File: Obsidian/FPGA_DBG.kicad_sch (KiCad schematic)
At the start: 24 parts, among them Q3 BSS138LT1G, SW1 SW_DIP_x01, U1 XC7A35T-CSG325, U27 W25Q128JVFIQ, U9 REF3012

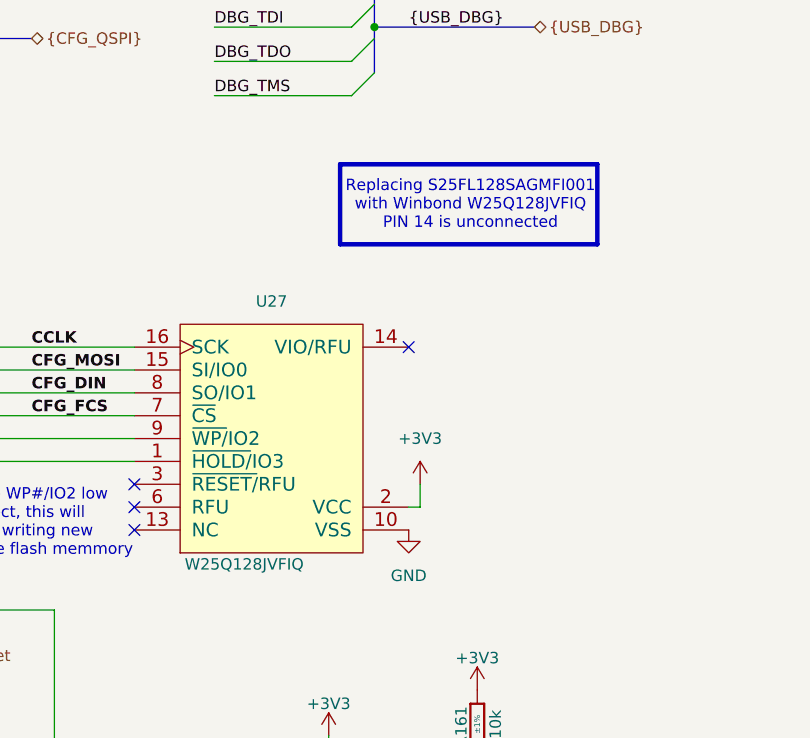
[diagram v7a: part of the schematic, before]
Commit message: Putting back S25FL128SAGMFI001 in FPGA_DBG sheet, see #17
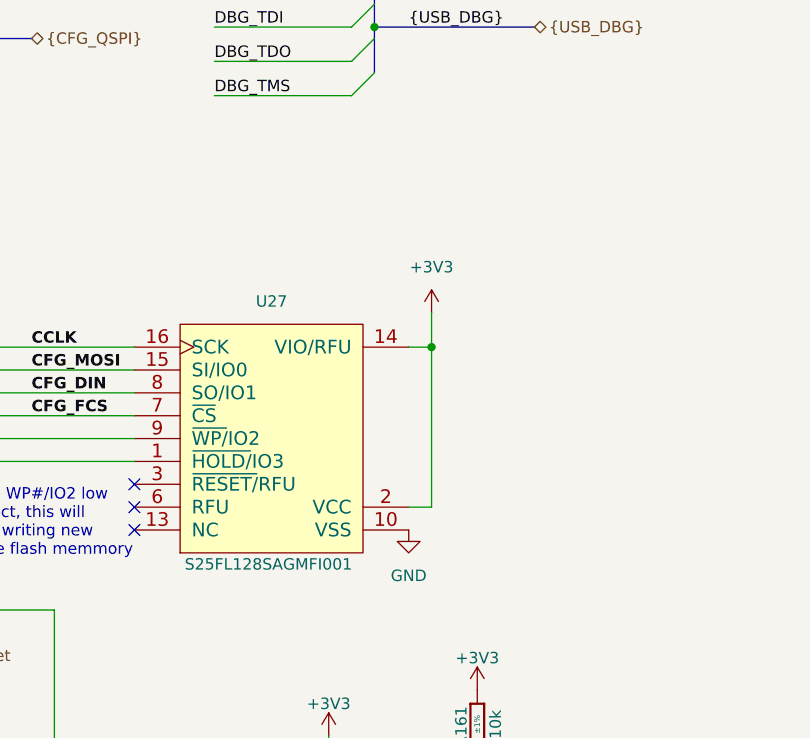
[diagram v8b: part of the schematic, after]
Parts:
- U27: value W25Q128JVFIQ -> S25FL128SAGMFI001; LCSC C111478 -> C466853; Library Ref W25Q128JVFIQ -> S25FL128SAGMFI001; Part Number W25Q128JVFIQ -> S25FL128SAGMFI001
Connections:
- net +3V3: now also U27.14 (VIO/RFU)
- no-connect marks 4 -> 3
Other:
- note removed: "Replacing S25FL128SAGMFI001 with Winbond W25Q128JVFIQ PIN 14 is unconnected"
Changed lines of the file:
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@@
 		(members "CFG_MOSI" "CFG_DIN" "CFG_FCS")
 	)
-	(rectangle
-		(start 238.76 44.45)
-		(end 267.335 53.34)
-		(stroke
-			(width 0.5)
-			(type solid)
-			(color 255 0 0 1)
-		)
-		(fill
-			(type none)
-		)
-	)
 	(text "FPGA DONE"
 		(exclude_from_sim no)
@@
 		)
 	)
-	(text "Replacing S25FL128SAGMFI001 \nwith Winbond W25Q128JVFIQ\nPIN 14 is unconnected"
-		(exclude_from_sim no)
-		(at 253.238 49.022 0)
-		(effects
-			(font
-				(size 1.27 1.27)
-			)
-		)
-	)
 	(text "- Configuration straps, according to AMD XAPP586 application note :\n CFGBVS_0 = 1 and M[2:0] = 001 (M2=0, M1=0, M0=1), selecting 3.3 V Master SPI boot mode.\n\n- PROGRAM_B_0 is pulled high. Driving this pin low asserts \nthe reset and restarts FPGA configuration. (see XAPP1313 application note p. 5)\n\n- A low level indicates initialization in progress, when initialization is complete it\nbecomes open-drain. This pin can be pulled high (see XAPP586, figure 4 p.7) "
 		(exclude_from_sim no)
@@
 	)
 	(junction
+		(at 248.92 64.77)
+		(diameter 0)
+		(color 0 0 0 0)
+	)
+	(junction
 		(at 200.66 138.43)
 		(diameter 0)
@@
 	)
 	(no_connect
-		(at 246.38 64.77)
-	)
-	(no_connect
 		(at 215.9 82.55)
 	)
@@
 	(wire
 		(pts
-			(xy 247.65 82.55) (xy 246.38 82.55)
+			(xy 189.23 55.88) (xy 189.23 74.93)
 		)
 		(stroke
@@
 	(wire
 		(pts
-			(xy 189.23 55.88) (xy 189.23 74.93)
+			(xy 237.49 124.46) (xy 247.65 124.46)
 		)
 		(stroke
@@
 	(wire
 		(pts
-			(xy 237.49 124.46) (xy 247.65 124.46)
+			(xy 160.02 138.43) (xy 167.64 138.43)
 		)
 		(stroke
@@
 	(wire
 		(pts
-			(xy 160.02 138.43) (xy 167.64 138.43)
+			(xy 157.48 130.81) (xy 160.02 130.81)
 		)
 		(stroke
@@
 	(wire
 		(pts
-			(xy 157.48 130.81) (xy 160.02 130.81)
+			(xy 195.58 77.47) (xy 195.58 55.88)
 		)
 		(stroke
@@
 	(wire
 		(pts
-			(xy 195.58 77.47) (xy 195.58 55.88)
+			(xy 171.45 35.56) (xy 184.15 35.56)
 		)
 		(stroke
@@
 	(wire
 		(pts
-			(xy 171.45 35.56) (xy 184.15 35.56)
+			(xy 207.01 124.46) (xy 237.49 124.46)
 		)
 		(stroke
@@
 	(wire
 		(pts
-			(xy 207.01 124.46) (xy 237.49 124.46)
+			(xy 248.92 64.77) (xy 248.92 82.55)
 		)
 		(stroke
@@
 	(wire
 		(pts
+			(xy 246.38 82.55) (xy 248.92 82.55)
+		)
+		(stroke
+			(width 0)
+			(type default)
+		)
+	)
+	(wire
+		(pts
 			(xy 207.01 93.98) (xy 207.01 124.46)
 		)
@@
 	(wire
 		(pts
+			(xy 246.38 64.77) (xy 248.92 64.77)
+		)
+		(stroke
+			(width 0)
+			(type default)
+		)
+	)
+	(wire
+		(pts
 			(xy 121.92 81.28) (xy 154.94 81.28)
 		)
@@
 	(wire
 		(pts
-			(xy 247.65 80.01) (xy 247.65 82.55)
+			(xy 248.92 60.96) (xy 248.92 64.77)
 		)
 		(stroke
@@
 			)
 		)
-		(property "Value" "W25Q128JVFIQ"
+		(property "Value" "S25FL128SAGMFI001"
 			(at 221.488 88.9 0)
 			(effects
@@
 			)
 		)
-		(property "Datasheet" "https://www.lcsc.com/datasheet/C111478.pdf"
+		(property "Datasheet" "https://www.lcsc.com/datasheet/C466853.pdf?spm=wm.sxq.inf.ggs___wm.ssy.bg.0.xh&lcsc_vid=RANdUwBXRwRaAVMCFAdWVwFUTwJWV1dXRVZcX1JVQwMxVlNRQFFaVFdTR1lYXjsOAxUeFF5JWBYZEEoKFBINSQcJGk4eFQsCAgIaSgADAwAHC0slT1dfVlVVWQkaCgg%3D"
 			(at 220.98 95.885 0)
 			(effects
@@
 			)
 		)
-		(property "Part Number" "W25Q128JVFIQ "
+		(property "Part Number" "S25FL128SAGMFI001"
 			(at 220.98 97.79 0)
 			(effects
@@
 			)
 		)
-		(property "Library Ref" "W25Q128JVFIQ "
+		(property "Library Ref" "S25FL128SAGMFI001"
 			(at 220.98 99.695 0)
 			(effects
@@
 			)
 		)
-		(property "LCSC" "C111478"
+		(property "LCSC" "C466853"
 			(at 220.98 62.23 0)
 			(effects
@@
 	(symbol
 		(lib_id "Library_Symbol:+1V0")
-		(at 247.65 80.01 0)
+		(at 248.92 60.96 0)
 		(unit 1)
 		(exclude_from_sim no)
@@
 		(fields_autoplaced yes)
 		(property "Reference" "#PWR0130"
-			(at 247.65 83.82 0)
+			(at 248.92 64.77 0)
 			(effects
 				(font
@@
 		)
 		(property "Value" "+3V3"
-			(at 247.65 74.93 0)
+			(at 248.92 55.88 0)
 			(effects
 				(font
@@
 		)
 		(property "Footprint" ""
-			(at 247.65 80.01 0)
+			(at 248.92 60.96 0)
 			(effects
 				(font
@@
 		)
 		(property "Datasheet" ""
-			(at 247.65 80.01 0)
+			(at 248.92 60.96 0)
 			(effects
 				(font
@@
 		)
 		(property "Description" "Power symbol creates a global label with name \"+1V0\""
-			(at 247.65 80.01 0)
+			(at 248.92 60.96 0)
 			(effects
 				(font
